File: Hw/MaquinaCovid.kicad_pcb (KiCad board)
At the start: 2 copper layers, 100 x 100 mm, 57 parts, among them J1 HC-SR04, J10 Screw_Terminal_01x03, J11 Screw_Terminal_01x03, J2 FTDI, J3 LCD, J4 MLX90614, J5 DS1307, J6 SD, J7 Screw_Terminal_01x02, J8 Screw_Terminal_01x11, J9 Screw_Terminal_01x11, Q1 MMBT2222A, Q2 MMBT2222A, Q3 MMBT2222A, SW1 RST, SW2 BOOT, SW3 Extra, U1 AZ1084CD-5.0TRG1, U2 AP2114H-3.3TRG1, U3 ESP32-WROOM-32, U4 LTV-817, U5 LTV-817, Y1 UD2-3NU, Y2 UD2-3NU

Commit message: Finished PCB
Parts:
- added H5: MountingHole, MountingHole:MountingHole_3.2mm_M3_Pad_Via, F.Cu at (55.8, 92.4)
- D4, D5, D6: footprint LED_THT:LED_D10.0mm -> Connector_PinHeader_2.54mm:PinHeader_1x02_P2.54mm_Vertical
- moved D4 131.5 mm to (46.5, 39.4), turned to 270 degrees
- moved C5 130.5 mm to (56.7, 77.1), turned to 270 degrees
- moved D7 129.0 mm to (62.6, 27.0), turned to 90 degrees
- moved R5 126.9 mm to (40.1, 2.76), turned to 90 degrees
- moved R2 123.1 mm to (44.1, 24.9), turned to 180 degrees
- moved R3 122.6 mm to (44.1, 26.9), turned to 180 degrees
- moved R4 120.5 mm to (44.1, 28.9), turned to 180 degrees
- moved D6 118.3 mm to (46.5, 32.1), turned to 270 degrees
- moved R6 106.2 mm to (62.6, 23.0), turned to 270 degrees
- moved Y2 106.0 mm to (39.8, 45.3), turned to 270 degrees
- moved D5 105.2 mm to (46.5, 35.7), turned to 270 degrees
- moved D8 98.7 mm to (47.0, 48.1), turned to 270 degrees
- moved Q3 96.7 mm to (43.0, 50.3)
- moved R14 91.2 mm to (43.2, 45.5)
- moved Y1 86.1 mm to (39.8, 59.9), turned to 270 degrees
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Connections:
- J8 pad 1: +5V -> /SCL
- J8 pad 2: GND -> /SDA
- J8 pad 3: /TX2 -> /RX2
- J8 pad 4: /RX2 -> /TX2
- J8 pad 5: /SDA -> GND
- J8 pad 6: /SCL -> +5V
- U3 pad 10: /L3 -> /Trig
- U3 pad 11: /L2 -> /Echo
- U3 pad 12: /Ry1 -> /L1
- U3 pad 13: /Buz -> /L2
- U3 pad 14: /Trig -> /L3
- U3 pad 16: /Echo -> /Ry1
- U3 pad 18: Net-(U3-Pad18) -> /Buz
- U3 pad 23: /L1 -> Net-(U3-Pad23)
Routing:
- net +5V: track 0.00 -> 201.7 mm
- net /SDA: track 0.00 -> 180.9 mm, vias 0 -> 2
- net /SCL: track 0.00 -> 175.6 mm, vias 0 -> 3
- net +3V3: track 9.39 -> 142.9 mm, vias 0 -> 7
- net /RX2: track 0.00 -> 101.6 mm, vias 0 -> 1
- net /TX2: track 0.00 -> 95.1 mm, vias 0 -> 1
- net GND: track 0.00 -> 94.0 mm, vias 0 -> 41
- net +12V: track 28.6 -> 108.3 mm, vias 0 -> 4
- net /Ry2: track 0.00 -> 53.3 mm, vias 0 -> 2
- net /Buz: track 0.00 -> 51.1 mm, vias 0 -> 2
- net /MOSI: track 0.00 -> 40.1 mm, vias 0 -> 1
- net /Ry1: track 0.00 -> 37.4 mm, vias 0 -> 2
- net /CS: track 0.00 -> 34.8 mm
- net /SCK: track 0.00 -> 33.8 mm
- net /MISO: track 0.00 -> 30.0 mm
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- added copper zone on B.Cu, net +3V3
- added copper zone on F.Cu, net +3V3
- added copper zone on B.Cu, net /PS
- added copper zone on B.Cu, net GND
- added copper zone on F.Cu, net GND
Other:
- net class V+ added: clearance 0.2, trace_width 0.5, via_dia 0.8, via_drill 0.4

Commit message: Add v1.0
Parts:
- added G***: LOGO, Aesthetics:electronic_cats_logo_8x6, B.Cu at (122.8, 122.7)
- added G***: LOGO, Aesthetics:electronic_cats_logo_8x6, F.Cu at (139.9, 76.1)
- added svg2mod: electronic, Aesthetics:titule_electronic_large, B.Cu at (146.8, 77.4)
- moved D1 85.8 mm to (139.3, 117.2)
- moved D3 85.8 mm to (135.2, 116.2)
- moved J4 85.8 mm to (175.5, 37.8)
- moved J5 85.8 mm to (189.4, 90.3)
- moved J6 85.8 mm to (156.5, 74.2)
- moved Q1 85.8 mm to (132.0, 115.1)
- moved U2 85.8 mm to (141.1, 104.0)
- moved BZ1 85.8 mm to (117.0, 127.4)
- moved C1 85.8 mm to (147.4, 102.2)
- moved C3 85.8 mm to (135.2, 107.8)
- moved C5 85.8 mm to (135.2, 111.9)
- moved D2 85.8 mm to (162.2, 41.0)
- moved D4 85.8 mm to (125.0, 74.1)
- moved D5 85.8 mm to (125.0, 70.5)
- moved D6 85.8 mm to (125.0, 66.8)
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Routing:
- net GND: track 94.0 -> 235.5 mm, vias 41 -> 93
- net +3V3: track 142.9 -> 243.6 mm, vias 7 -> 9
- net /COM2: track 21.6 -> 39.7 mm
- net /COM1: track 18.4 -> 36.3 mm
- net +5V: track 201.7 -> 215.4 mm
- net +12V: track 108.3 -> 117.2 mm
- net /NC2: track 14.6 -> 18.8 mm
- net /PS: track 26.6 -> 30.1 mm
- net /NC1: track 13.9 -> 16.7 mm
- net /SCL: track 175.6 -> 178.0 mm
- net /SDA: track 180.9 -> 182.4 mm, vias 2 -> 0
- net /Buz: track 51.1 -> 52.5 mm
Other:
- net class Default: trace_width 0.5 -> 0.3
- board text added: "12v"
- board text added: "GND"
- board text added: "MediTemp-C"
- board text added: "V1.0"

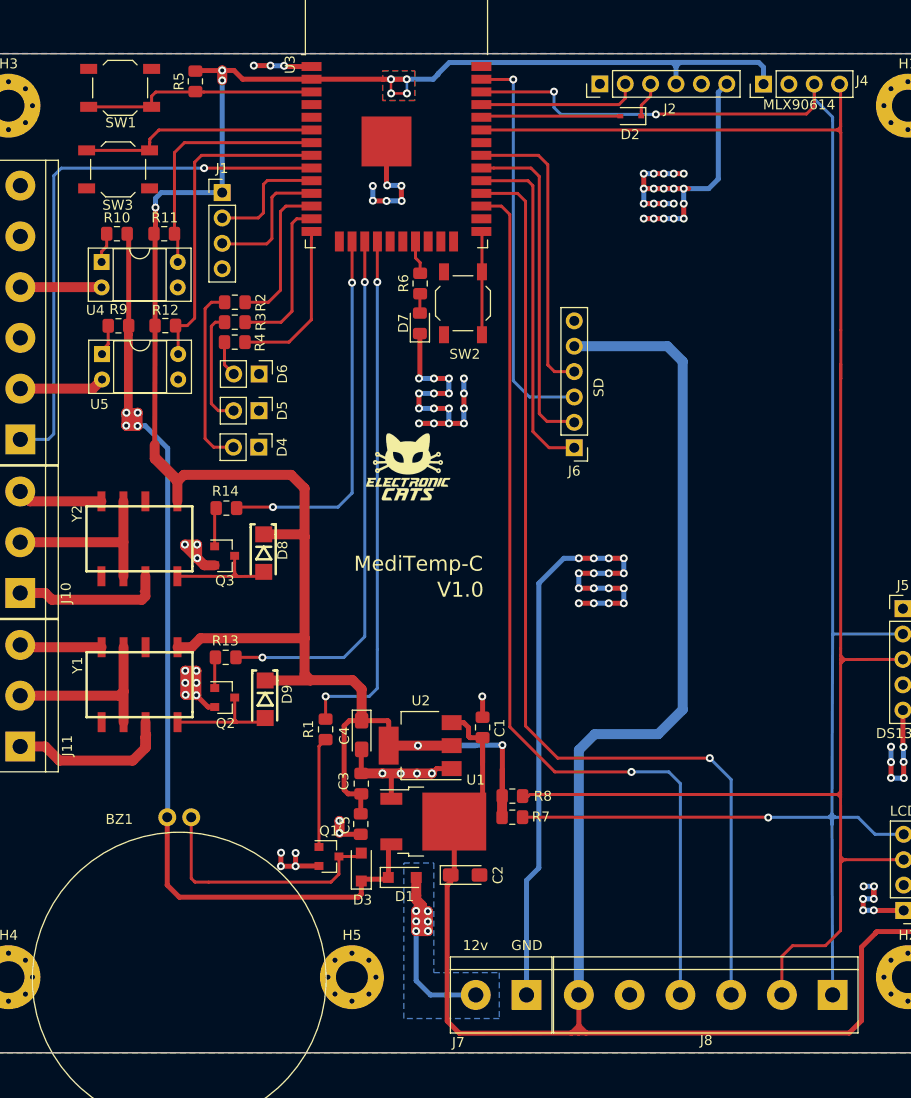
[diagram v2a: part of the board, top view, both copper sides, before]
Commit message: Covid machine V1.1
-Added pull-up to the boot button
-Change of the conection of the buzzer and relay pines
-Added 5v to the ultrasonic sensor
-Removed the diode on FTDI's TX pin
-Added missing names on the componens
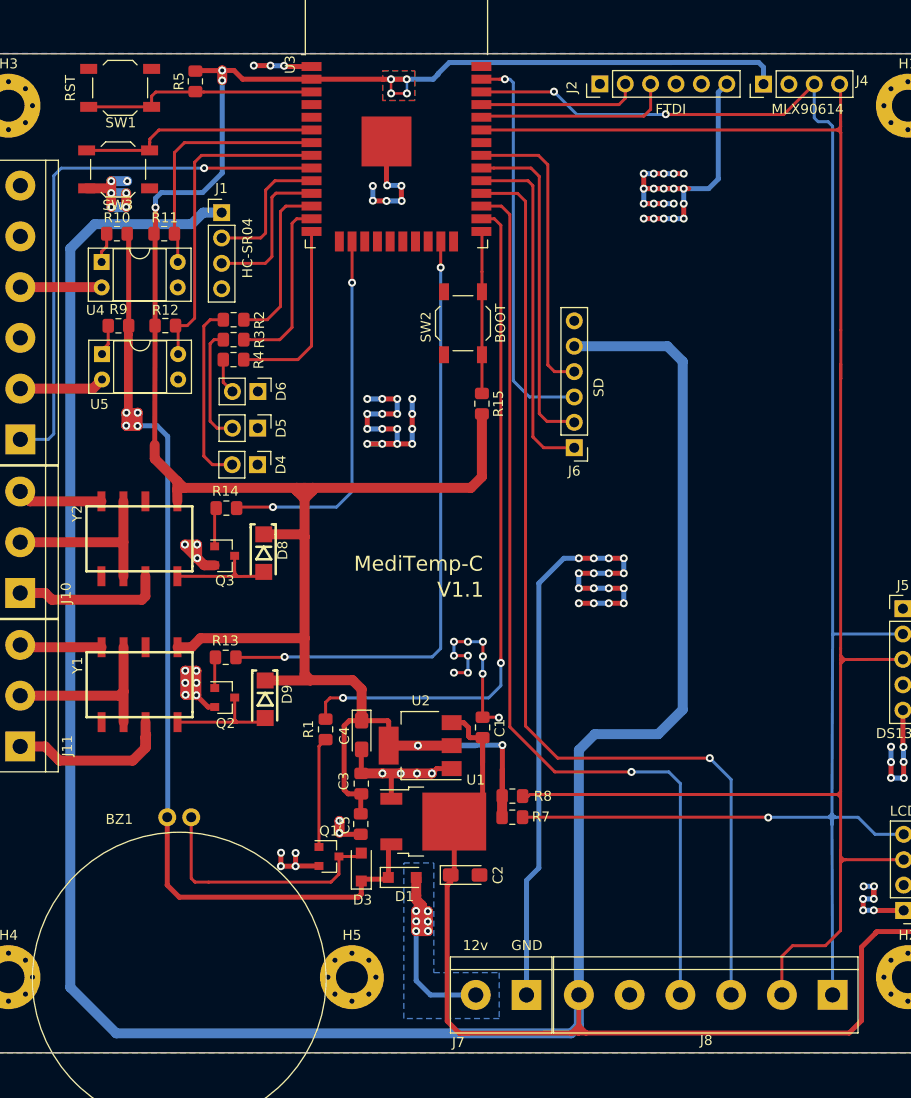
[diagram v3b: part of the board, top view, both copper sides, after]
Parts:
- removed D2: 1N4148, Diode_SMD:D_SOD-323
- removed D7: LED, LED_SMD:LED_0805_2012Metric_Pad1.15x1.40mm_HandSolder
- removed G*** (x2): LOGO, Aesthetics:electronic_cats_logo_8x6
- removed R6: 330, Resistor_SMD:R_0805_2012Metric_Pad1.15x1.40mm_HandSolder
- removed svg2mod: electronic, Aesthetics:titule_electronic_large
- added R15: 10K, Resistor_SMD:R_0805_2012Metric_Pad1.15x1.40mm_HandSolder, F.Cu at (147.3, 69.8)
- moved J1 2.00 mm to (121.2, 50.6)
- moved SW2 2.00 mm to (145.4, 61.7)
- moved D4 1.75 mm to (124.8, 75.9)
- moved D5 1.75 mm to (124.9, 72.2)
- moved D6 1.75 mm to (124.9, 68.6)
- moved R2 1.75 mm to (122.4, 61.4)
- moved R3 1.75 mm to (122.4, 63.4)
- moved R4 1.75 mm to (122.4, 65.4)
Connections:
- J1 pad 1: +3V3 -> +5V
- J2 pad 3: Net-(D2-Pad1) -> /TX
- J2 pad 4: +3V3 -> Net-(J2-Pad4)
- U3 pad 17: /Ry2 -> Net-(U3-Pad17)
- U3 pad 18: /Buz -> Net-(U3-Pad18)
- U3 pad 21: /L4 -> Net-(U3-Pad21)
- U3 pad 23: Net-(U3-Pad23) -> /Ry2
- U3 pad 26: Net-(U3-Pad26) -> /Buz
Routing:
- net +5V: track 215.4 -> 362.2 mm
- net GND: track 235.5 -> 258.0 mm, vias 93 -> 108
- net +3V3: track 243.6 -> 261.6 mm
- net /Buz: track 52.5 -> 68.2 mm
- net /Ry2: track 53.3 -> 61.6 mm
- net /GPIO0: track 10.4 -> 16.2 mm
- net /TX: track 14.0 -> 19.8 mm
- net Net-(D2-Pad1): track 3.61 -> 0.00 mm
- net /L4: track 3.37 -> 0.00 mm
- net /L3: track 16.4 -> 18.8 mm
- net Net-(D7-Pad2): track 1.95 -> 0.00 mm
- net /Echo: track 13.7 -> 15.6 mm
- net /L2: track 16.1 -> 17.9 mm
- net /L1: track 15.2 -> 17.1 mm
- net /Trig: track 12.3 -> 14.0 mm
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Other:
- board text added: "V1.1"
